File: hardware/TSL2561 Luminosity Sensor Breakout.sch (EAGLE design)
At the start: 14 parts, among them U1 TSL2561T

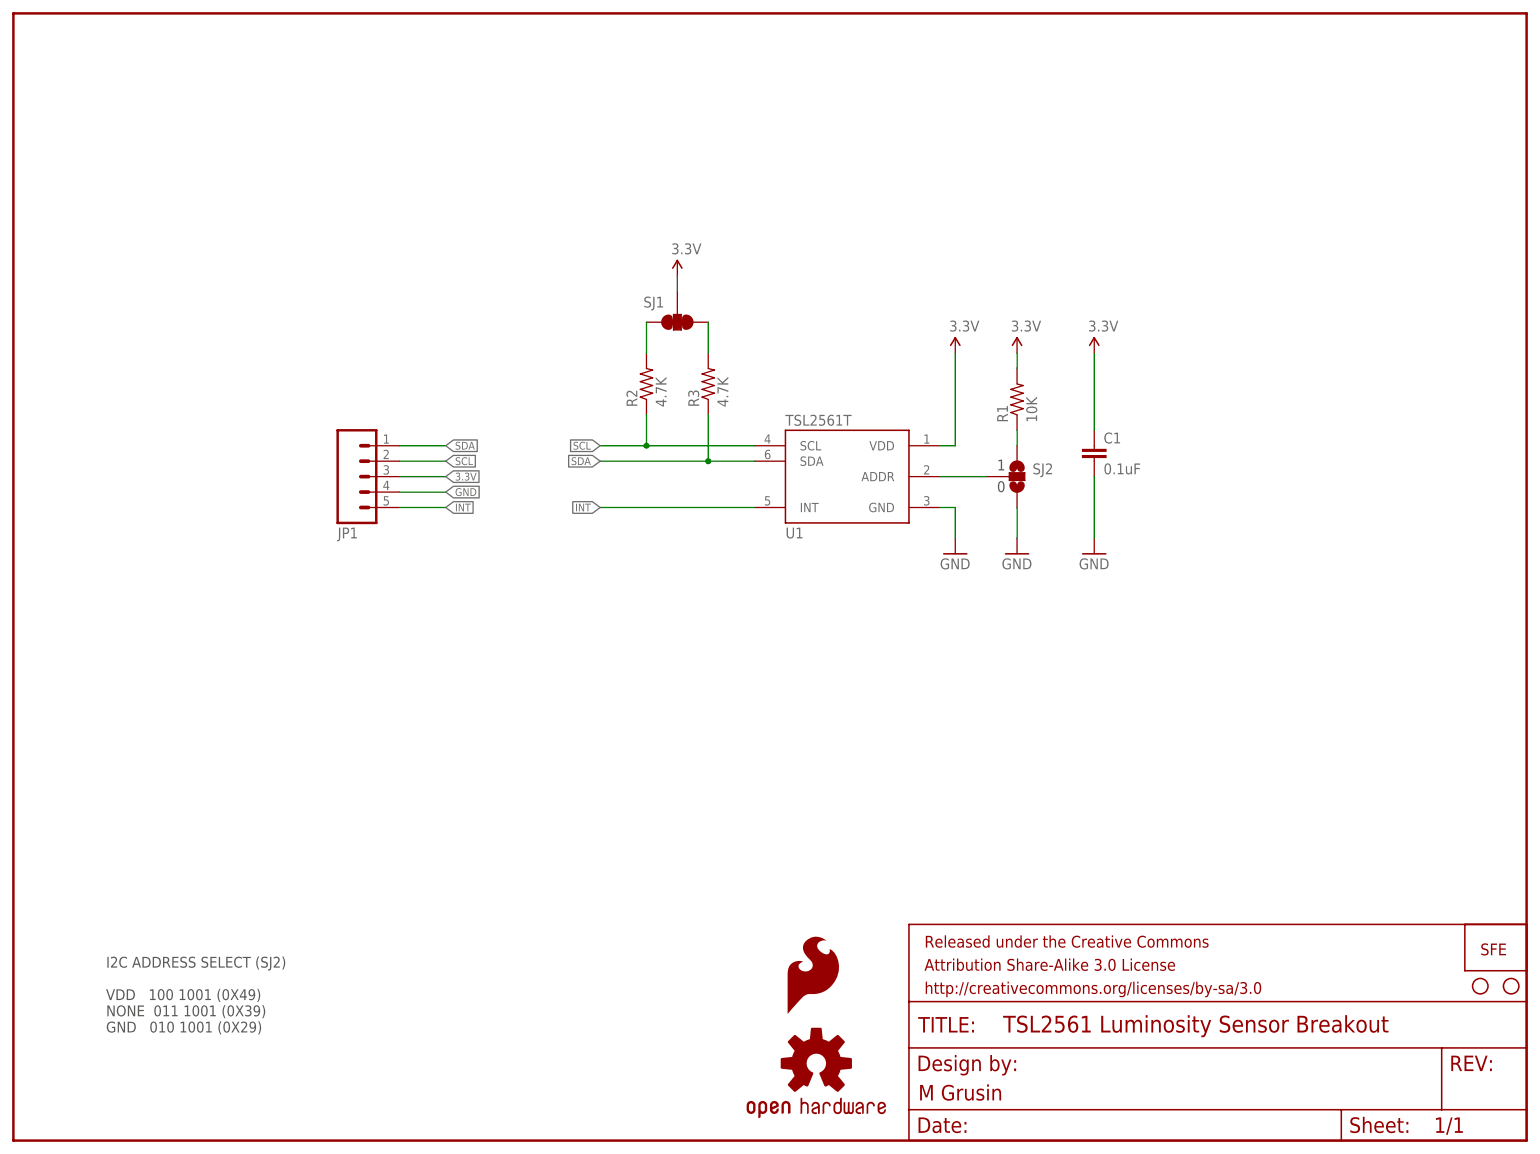
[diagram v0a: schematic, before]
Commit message: Updated prototype to V02
Per discussion with Pete L, replaced T package with FN package.
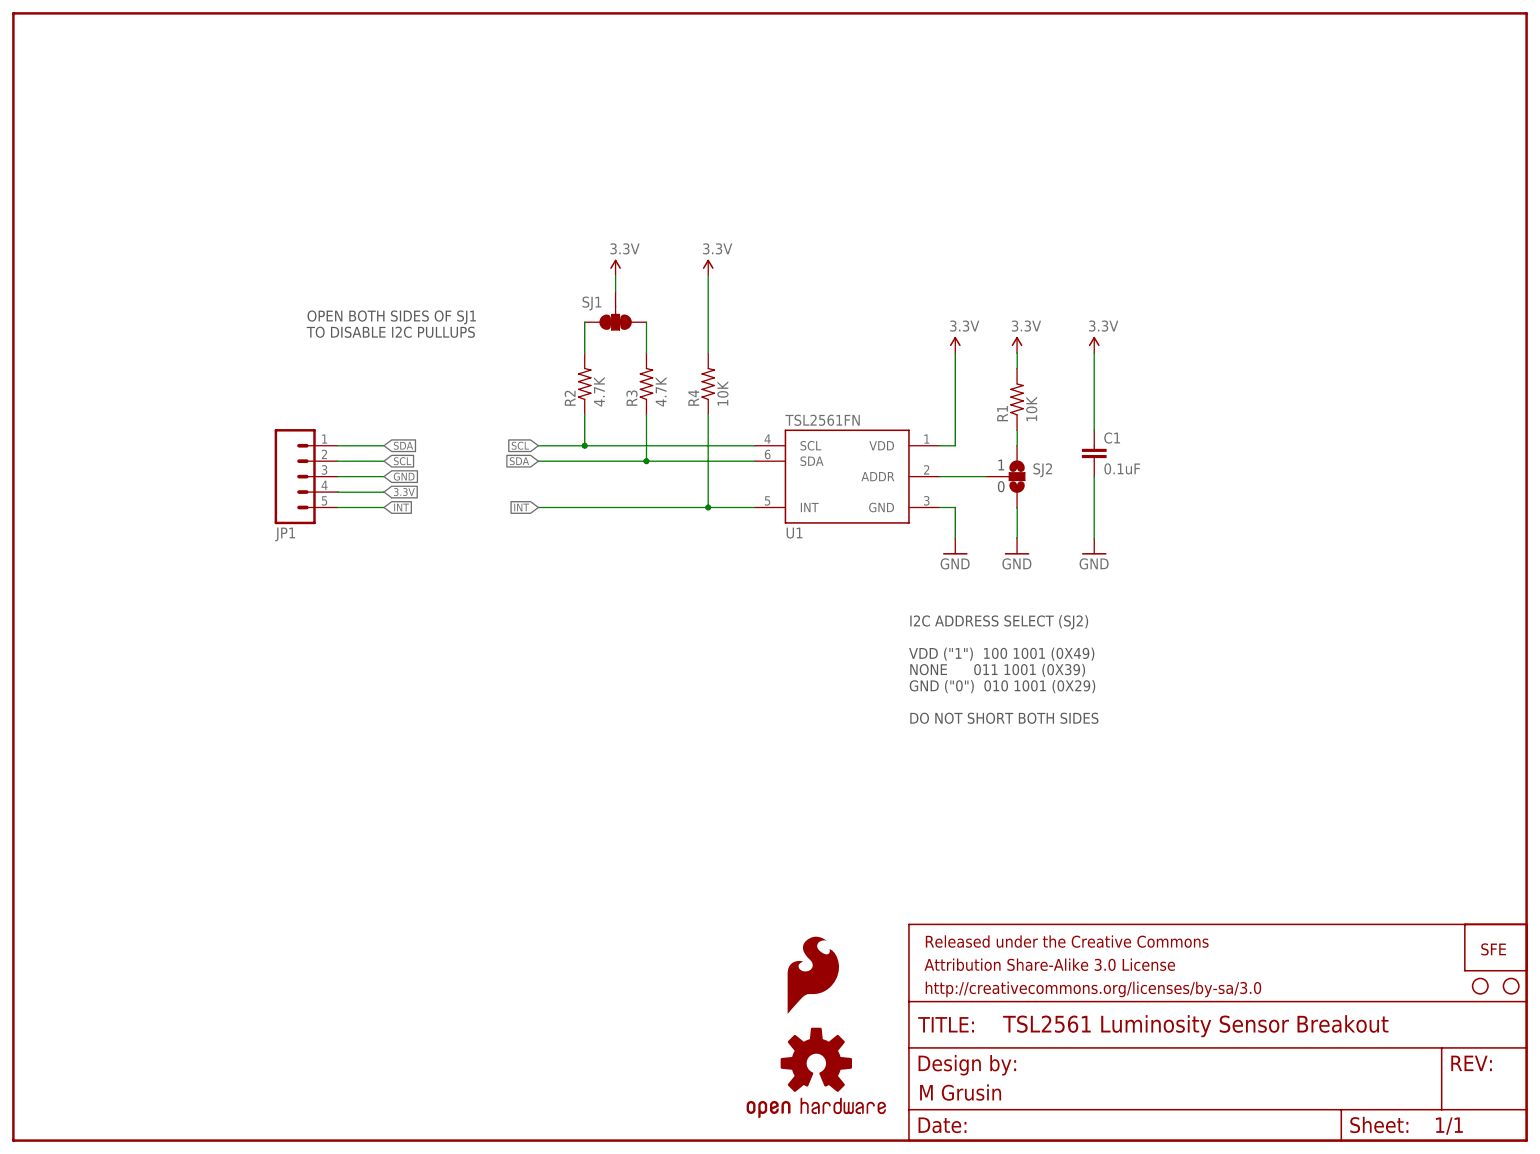
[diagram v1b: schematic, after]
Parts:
- added R4: 10K, SparkFun-Resistors:RESISTOR0603
- U1: value TSL2561T -> TSL2561FN; device mike-temp:TSL2561T -> mike-temp:TSL2561FN
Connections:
- net 3.3V: now also JP1.4, R4.2; no longer JP1.3
- net GND: now also JP1.3; no longer JP1.4
- net INT: now also R4.1
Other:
- note added: "I2C ADDRESS SELECT (SJ2) VDD ("1") 100 1001 (0X49) NONE 011 1001 (0X39) GND ("0") 010 1001 (0X29) DO NOT SHORT BOTH SIDES"
- note added: "OPEN BOTH SIDES OF SJ1 TO DISABLE I2C PULLUPS"
- note removed: "I2C ADDRESS SELECT (SJ2) VDD 100 1001 (0X49) NONE 011 1001 (0X39) GND 010 1001 (0X29)"
- moved on the sheet: JP1, R2, R3, SJ1
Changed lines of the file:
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@@
 <parts>
 <part name="FRAME1" library="SparkFun-Aesthetics" deviceset="FRAME-LETTER" device=""/>
-<part name="U1" library="mike-temp" deviceset="TSL2561" device="T"/>
+<part name="U1" library="mike-temp" deviceset="TSL2561" device="FN" value="TSL2561FN"/>
 <part name="SJ1" library="mike-temp" deviceset="SOLDERJUMPER_2WAY" device="PASTE1&amp;2&amp;3"/>
 <part name="SJ2" library="mike-temp" deviceset="SOLDERJUMPER_2WAY" device="S"/>
@@
 <part name="STANDOFF2" library="SparkFun-Electromechanical" deviceset="STAND-OFF" device=""/>
 <part name="LOGO3" library="SparkFun-Aesthetics" deviceset="SFE_LOGO_FLAME" device=".1_INCH" value="SFE_LOGO_FLAME.1_INCH"/>
+<part name="R4" library="SparkFun-Resistors" deviceset="RESISTOR" device="0603" value="10K"/>
+<part name="SUPPLY5" library="SparkFun-Aesthetics" deviceset="VCC" device="" value="3.3V"/>
 </parts>
 <sheets>
 <sheet>
 <plain>
-<rectangle x1="107.188" y1="134.112" x2="110.998" y2="135.128" layer="94"/>
+<rectangle x1="97.028" y1="134.112" x2="100.838" y2="135.128" layer="94"/>
 <text x="161.798" y="110.236" size="1.778" layer="97">1</text>
 <text x="161.798" y="106.68" size="1.778" layer="97">0</text>
-<text x="15.24" y="17.78" size="1.778" layer="97">I2C ADDRESS SELECT (SJ2)
-VDD   100 1001 (0X49)
-NONE  011 1001 (0X39)
-GND   010 1001 (0X29)</text>
+<text x="147.32" y="68.58" size="1.778" layer="97">I2C ADDRESS SELECT (SJ2)
+VDD ("1")  100 1001 (0X49)
+NONE      011 1001 (0X39)
+GND ("0")  010 1001 (0X29)
+DO NOT SHORT BOTH SIDES</text>
 <text x="148.844" y="6.604" size="2.54" layer="94" ratio="10">M Grusin</text>
+<text x="48.26" y="132.08" size="1.778" layer="97">OPEN BOTH SIDES OF SJ1
+TO DISABLE I2C PULLUPS</text>
 </plain>
 <instances>
@@
 <instance part="FRAME1" gate="G$2" x="147.32" y="0"/>
 <instance part="U1" gate="G$1" x="137.16" y="109.22"/>
-<instance part="SJ1" gate="G$1" x="109.22" y="134.62" smashed="yes" rot="R270">
-<attribute name="NAME" x="103.632" y="137.033" size="1.778" layer="95"/>
-<attribute name="VALUE" x="107.315" y="132.08" size="1.778" layer="96" rot="R270"/>
+<instance part="SJ1" gate="G$1" x="99.06" y="134.62" smashed="yes" rot="R270">
+<attribute name="NAME" x="93.472" y="137.033" size="1.778" layer="95"/>
+<attribute name="VALUE" x="97.155" y="132.08" size="1.778" layer="96" rot="R270"/>
 </instance>
 <instance part="SJ2" gate="G$1" x="165.1" y="109.22"/>
 <instance part="R1" gate="G$1" x="165.1" y="121.92" rot="R90"/>
-<instance part="R2" gate="G$1" x="104.14" y="124.46" rot="R90"/>
-<instance part="R3" gate="G$1" x="114.3" y="124.46" rot="R90"/>
+<instance part="R2" gate="G$1" x="93.98" y="124.46" rot="R90"/>
+<instance part="R3" gate="G$1" x="104.14" y="124.46" rot="R90"/>
 <instance part="C1" gate="G$1" x="177.8" y="111.76"/>
 <instance part="SUPPLY1" gate="1" x="154.94" y="129.54"/>
 <instance part="SUPPLY2" gate="1" x="165.1" y="129.54"/>
 <instance part="SUPPLY3" gate="1" x="177.8" y="129.54"/>
-<instance part="SUPPLY4" gate="1" x="109.22" y="142.24"/>
+<instance part="SUPPLY4" gate="1" x="99.06" y="142.24"/>
 <instance part="GND1" gate="1" x="165.1" y="96.52"/>
 <instance part="GND2" gate="1" x="177.8" y="96.52"/>
 <instance part="GND3" gate="1" x="154.94" y="96.52"/>
-<instance part="JP1" gate="G$1" x="55.88" y="109.22" rot="MR180"/>
+<instance part="JP1" gate="G$1" x="45.72" y="109.22" rot="MR180"/>
 <instance part="LOGO1" gate="G$1" x="132.08" y="12.7"/>
 <instance part="LOGO2" gate="G$1" x="241.3" y="30.48"/>
@@
 <instance part="STANDOFF2" gate="G$1" x="241.3" y="25.4"/>
 <instance part="LOGO3" gate="G$1" x="127" y="20.32"/>
+<instance part="R4" gate="G$1" x="114.3" y="124.46" rot="R90"/>
+<instance part="SUPPLY5" gate="1" x="114.3" y="142.24"/>
 </instances>
 <busses>
@@
 </segment>
 <segment>
-<pinref part="JP1" gate="G$1" pin="4"/>
-<wire x1="63.5" y1="106.68" x2="71.12" y2="106.68" width="0.1524" layer="91"/>
-<label x="71.12" y="106.68" size="1.27" layer="95" xref="yes"/>
+<pinref part="JP1" gate="G$1" pin="3"/>
+<wire x1="53.34" y1="109.22" x2="60.96" y2="109.22" width="0.1524" layer="91"/>
+<label x="60.96" y="109.22" size="1.27" layer="95" xref="yes"/>
 </segment>
 </net>
@@
 <pinref part="R3" gate="G$1" pin="2"/>
 <pinref part="SJ1" gate="G$1" pin="1"/>
-<wire x1="114.3" y1="129.54" x2="114.3" y2="134.62" width="0.1524" layer="91"/>
+<wire x1="104.14" y1="129.54" x2="104.14" y2="134.62" width="0.1524" layer="91"/>
 </segment>
 </net>
@@
 <pinref part="R2" gate="G$1" pin="2"/>
 <pinref part="SJ1" gate="G$1" pin="3"/>
-<wire x1="104.14" y1="129.54" x2="104.14" y2="134.62" width="0.1524" layer="91"/>
+<wire x1="93.98" y1="129.54" x2="93.98" y2="134.62" width="0.1524" layer="91"/>
 </segment>
 </net>
@@
 <segment>
 <pinref part="JP1" gate="G$1" pin="1"/>
-<wire x1="63.5" y1="114.3" x2="71.12" y2="114.3" width="0.1524" layer="91"/>
-<label x="71.12" y="114.3" size="1.27" layer="95" xref="yes"/>
+<wire x1="53.34" y1="114.3" x2="60.96" y2="114.3" width="0.1524" layer="91"/>
+<label x="60.96" y="114.3" size="1.27" layer="95" xref="yes"/>
 </segment>
 <segment>
 <pinref part="R3" gate="G$1" pin="1"/>
-<wire x1="114.3" y1="119.38" x2="114.3" y2="111.76" width="0.1524" layer="91"/>
+<wire x1="104.14" y1="119.38" x2="104.14" y2="111.76" width="0.1524" layer="91"/>
 <pinref part="U1" gate="G$1" pin="SDA"/>
-<wire x1="114.3" y1="111.76" x2="121.92" y2="111.76" width="0.1524" layer="91"/>
-<wire x1="114.3" y1="111.76" x2="96.52" y2="111.76" width="0.1524" layer="91"/>
-<junction x="114.3" y="111.76"/>
-<label x="96.52" y="111.76" size="1.27" layer="95" rot="R180" xref="yes"/>
+<wire x1="104.14" y1="111.76" x2="121.92" y2="111.76" width="0.1524" layer="91"/>
+<wire x1="104.14" y1="111.76" x2="86.36" y2="111.76" width="0.1524" layer="91"/>
+<junction x="104.14" y="111.76"/>
+<label x="86.36" y="111.76" size="1.27" layer="95" rot="R180" xref="yes"/>
 </segment>
 </net>
@@
 <segment>
 <pinref part="JP1" gate="G$1" pin="2"/>
-<wire x1="63.5" y1="111.76" x2="71.12" y2="111.76" width="0.1524" layer="91"/>
-<label x="71.12" y="111.76" size="1.27" layer="95" xref="yes"/>
+<wire x1="53.34" y1="111.76" x2="60.96" y2="111.76" width="0.1524" layer="91"/>
+<label x="60.96" y="111.76" size="1.27" layer="95" xref="yes"/>
 </segment>
 <segment>
 <pinref part="U1" gate="G$1" pin="SCL"/>
-<wire x1="121.92" y1="114.3" x2="104.14" y2="114.3" width="0.1524" layer="91"/>
+<wire x1="121.92" y1="114.3" x2="93.98" y2="114.3" width="0.1524" layer="91"/>
 <pinref part="R2" gate="G$1" pin="1"/>
-<wire x1="104.14" y1="114.3" x2="104.14" y2="119.38" width="0.1524" layer="91"/>
-<wire x1="104.14" y1="114.3" x2="96.52" y2="114.3" width="0.1524" layer="91"/>
-<junction x="104.14" y="114.3"/>
-<label x="96.52" y="114.3" size="1.27" layer="95" rot="R180" xref="yes"/>
+<wire x1="93.98" y1="114.3" x2="93.98" y2="119.38" width="0.1524" layer="91"/>
+<wire x1="93.98" y1="114.3" x2="86.36" y2="114.3" width="0.1524" layer="91"/>
+<junction x="93.98" y="114.3"/>
+<label x="86.36" y="114.3" size="1.27" layer="95" rot="R180" xref="yes"/>
 </segment>
 </net>
 <net name="3.3V" class="0">
-<segment>
-<pinref part="JP1" gate="G$1" pin="3"/>
-<wire x1="63.5" y1="109.22" x2="71.12" y2="109.22" width="0.1524" layer="91"/>
-<label x="71.12" y="109.22" size="1.27" layer="95" xref="yes"/>
-</segment>
 <segment>
 <pinref part="U1" gate="G$1" pin="VDD"/>
@@
 <pinref part="SJ1" gate="G$1" pin="2"/>
 <pinref part="SUPPLY4" gate="1" pin="VCC"/>
-<wire x1="109.22" y1="142.24" x2="109.22" y2="139.7" width="0.1524" layer="91"/>
+<wire x1="99.06" y1="142.24" x2="99.06" y2="139.7" width="0.1524" layer="91"/>
+</segment>
+<segment>
+<pinref part="JP1" gate="G$1" pin="4"/>
+<wire x1="53.34" y1="106.68" x2="60.96" y2="106.68" width="0.1524" layer="91"/>
+<label x="60.96" y="106.68" size="1.27" layer="95" xref="yes"/>
+</segment>
+<segment>
+<pinref part="R4" gate="G$1" pin="2"/>
+<pinref part="SUPPLY5" gate="1" pin="VCC"/>
+<wire x1="114.3" y1="142.24" x2="114.3" y2="129.54" width="0.1524" layer="91"/>
 </segment>
 </net>
@@
 <segment>
 <pinref part="JP1" gate="G$1" pin="5"/>
-<wire x1="63.5" y1="104.14" x2="71.12" y2="104.14" width="0.1524" layer="91"/>
-<label x="71.12" y="104.14" size="1.27" layer="95" xref="yes"/>
+<wire x1="53.34" y1="104.14" x2="60.96" y2="104.14" width="0.1524" layer="91"/>
+<label x="60.96" y="104.14" size="1.27" layer="95" xref="yes"/>
 </segment>
 <segment>
 <pinref part="U1" gate="G$1" pin="INT"/>
-<wire x1="121.92" y1="104.14" x2="96.52" y2="104.14" width="0.1524" layer="91"/>
-<label x="96.52" y="104.14" size="1.27" layer="95" rot="R180" xref="yes"/>
-</segment>
-</net>
+<wire x1="121.92" y1="104.14" x2="114.3" y2="104.14" width="0.1524" layer="91"/>
+<label x="86.36" y="104.14" size="1.27" layer="95" rot="R180" xref="yes"/>
+<pinref part="R4" gate="G$1" pin="1"/>
+<wire x1="114.3" y1="104.14" x2="86.36" y2="104.14" width="0.1524" layer="91"/>
+<wire x1="114.3" y1="119.38" x2="114.3" y2="104.14" width="0.1524" layer="91"/>
+<junction x="114.3" y="104.14"/>
+</segment>
+</net>
